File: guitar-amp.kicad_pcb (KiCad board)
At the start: 2 copper layers, 135 x 90 mm, 62 parts, among them J1 Speaker Output, J2 Input, J3 AC Mains, J4 Screw_Terminal_01x02, J5 Screw_Terminal_01x02, J6 Screw_Terminal_01x02, SW1 SW_SPST, T1 Transformer_1P_1S

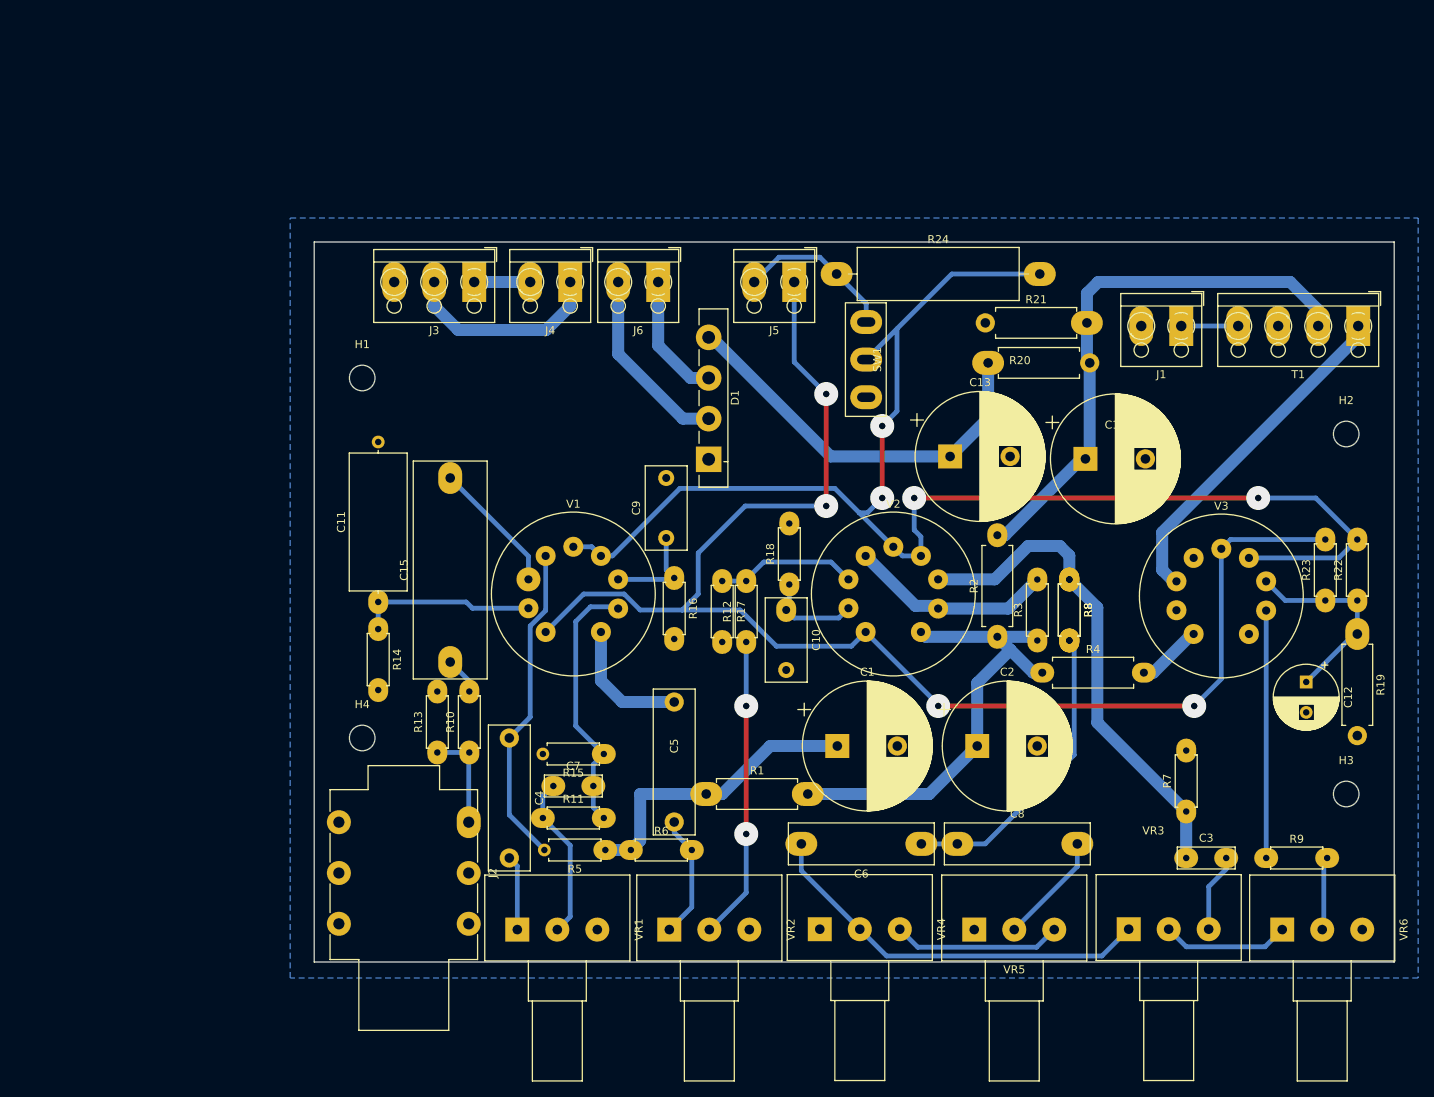
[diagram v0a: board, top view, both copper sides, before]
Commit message: update pads
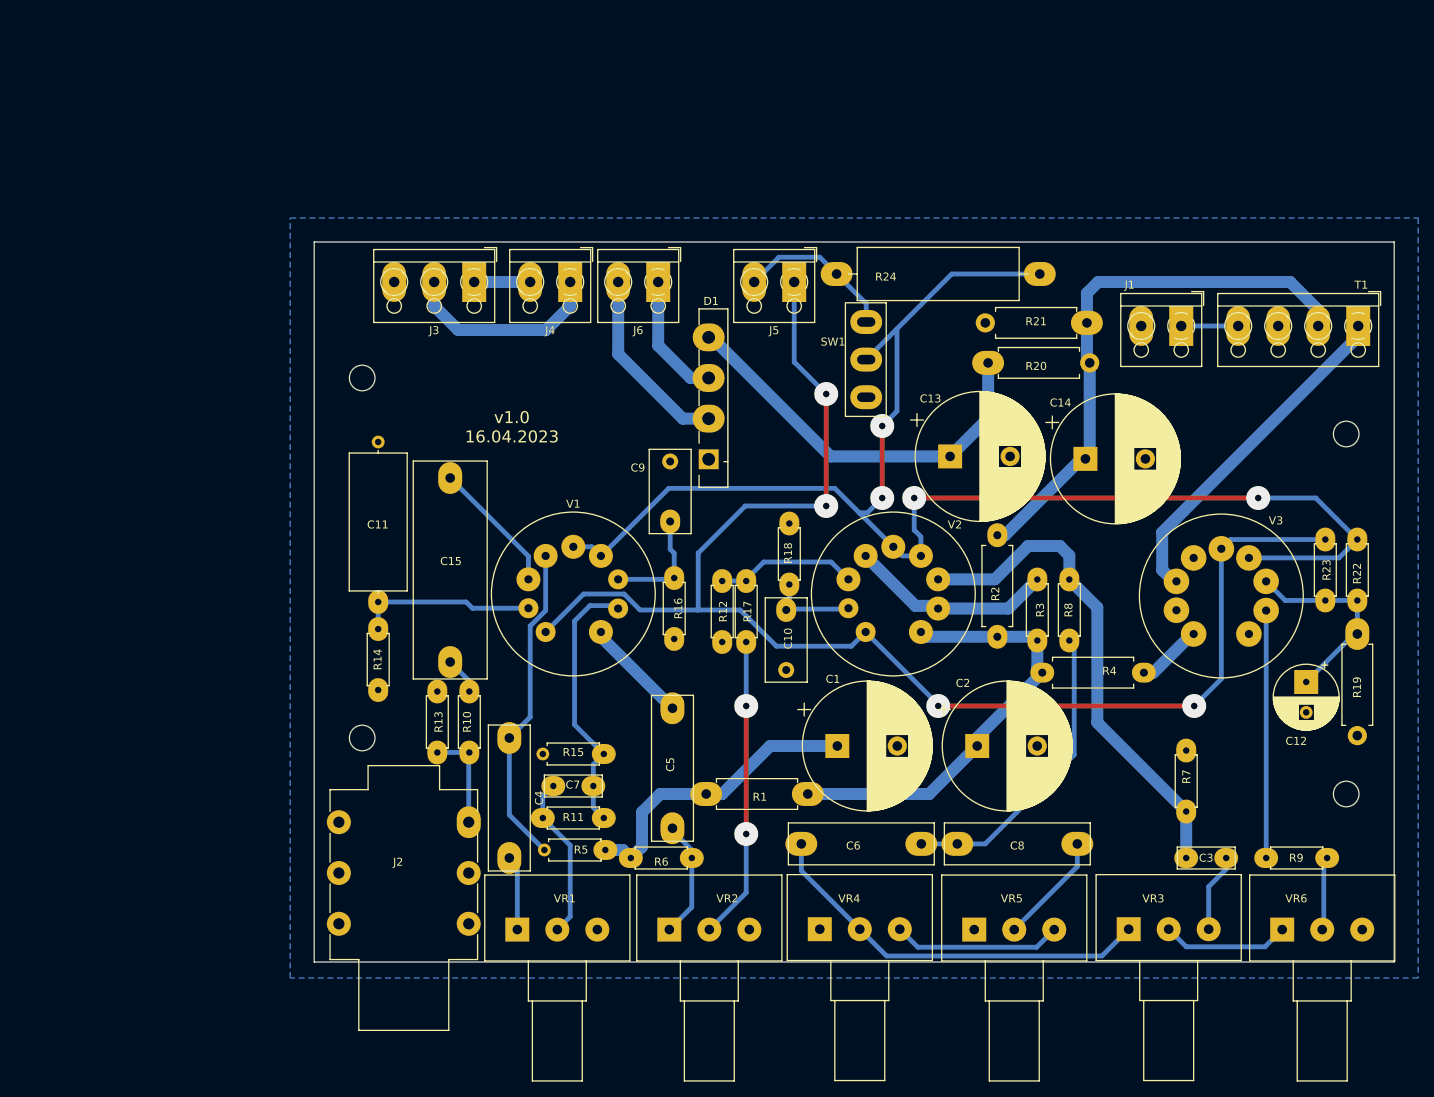
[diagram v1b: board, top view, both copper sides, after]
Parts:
- removed the R8 at (210.4, 92.2)
- moved C9 2.12 mm to (160.5, 84.9)
- moved R6 1.00 mm to (155.6, 127.0)
- moved C5 0.81 mm to (160.8, 108.3)
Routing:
- net /HighDC_241VDC: track 59.9 -> 55.5 mm
- net /HighDC_V1B_Anode: track 16.4 -> 13.2 mm
- net Net-(C9-Pad1): track 12.5 -> 14.4 mm
- net Net-(C10-Pad1): track 10.9 -> 10.0 mm
- net Net-(J5-Pad1): track 181.2 -> 180.4 mm
- net Net-(C5-Pad2): track 15.5 -> 14.8 mm
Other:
- board text added: "v1.0 16.04.2023"

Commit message: prepare for plotting
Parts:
- moved H2 10.0 mm to (246.0, 64.0)
- moved R9 7.81 mm to (235.0, 119.2), turned to -90 degrees
- moved H3 6.08 mm to (246.0, 125.0)
- moved J1 5.51 mm to (224.4, 55.0)
- moved T1 5.51 mm to (246.5, 55.0)
- moved R15 4.37 mm to (152.4, 118.4)
- moved C7 3.97 mm to (147.3, 114.3)
- moved H1 3.16 mm to (121.0, 64.0)
- moved H4 1.00 mm to (121.0, 112.0)
- moved R11 0.22 mm to (144.8, 121.9)
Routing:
- net Net-(R9-Pad1): track 30.9 -> 23.2 mm
- net /HighDC_OT: track 43.0 -> 48.3 mm
- net Net-(C7-Pad1): track 20.6 -> 25.6 mm
- net /HighDC_Post: track 68.9 -> 64.0 mm
- net Net-(R9-Pad2): track 9.21 -> 13.1 mm
- net Net-(C7-Pad2): track 33.6 -> 32.5 mm
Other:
- board text added: "Hole Size - All C and R 0.8 - Terminal sockets 1 - Potis 1 - Valves 1.02 - Bridge rectifier 1.2 - Jack socket 1.2"
- board text added: "TODO: - Buy 2 x 12AX7"

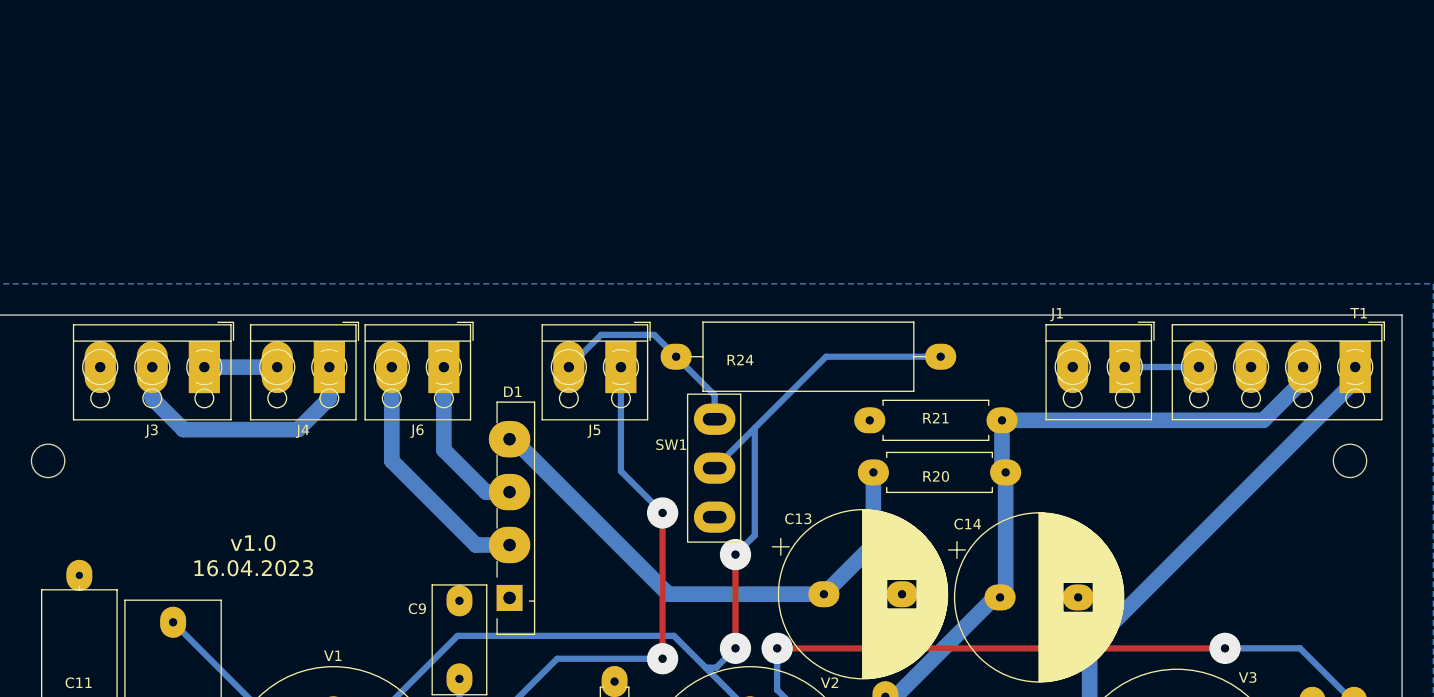
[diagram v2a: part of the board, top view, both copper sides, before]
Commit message: Add lamp and test points
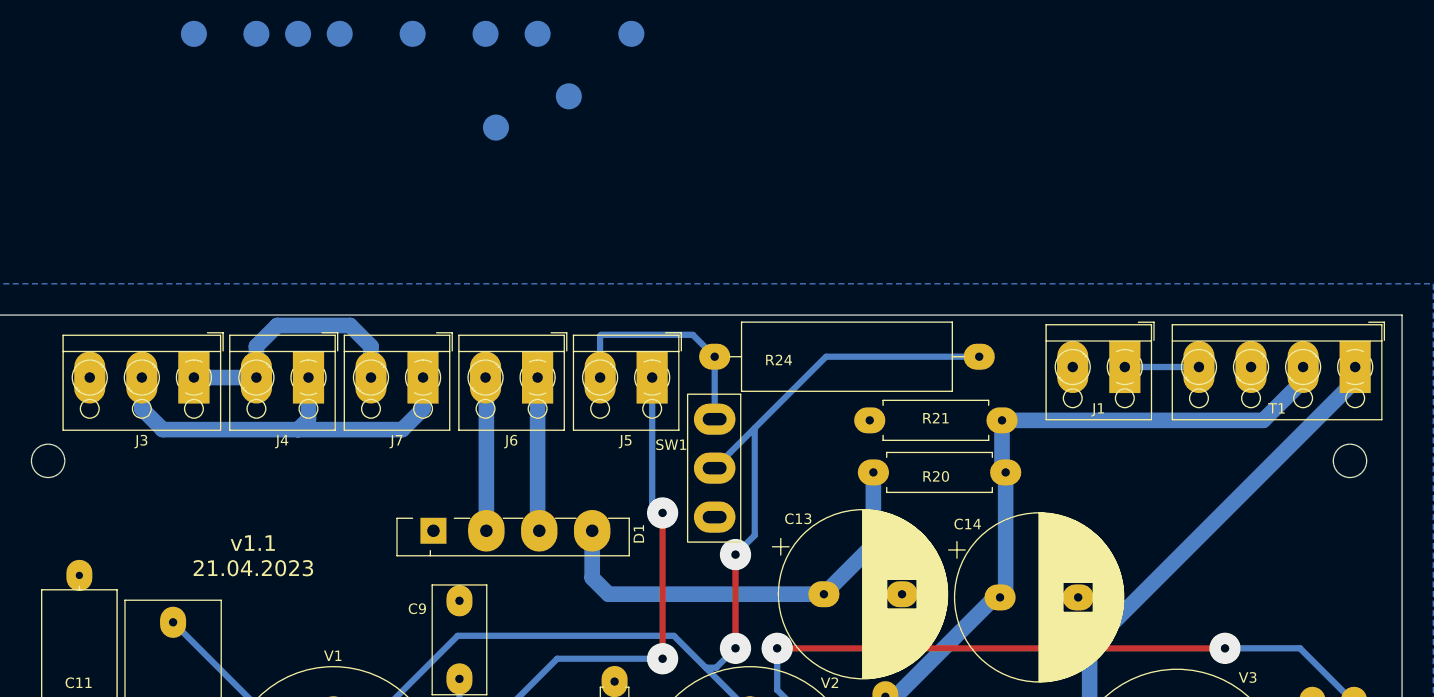
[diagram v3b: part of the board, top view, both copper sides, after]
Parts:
- added J7: Lamp, TerminalBlock_RND:TerminalBlock_RND_205-00001_1x02_P5.00mm_Horizontal, F.Cu at (157.0, 56.0)
- added TP1: TestPoint_Probe, TestPoint:TestPoint_Pad_D2.5mm, B.Cu at (135.0, 23.0)
- added TP10: TestPoint_Probe, TestPoint:TestPoint_Pad_D2.5mm, B.Cu at (177.0, 23.0)
- added TP2: TestPoint_Probe, TestPoint:TestPoint_Pad_D2.5mm, B.Cu at (141.0, 23.0)
- added TP3: TestPoint_Probe, TestPoint:TestPoint_Pad_D2.5mm, B.Cu at (145.0, 23.0)
- added TP4: TestPoint_Probe, TestPoint:TestPoint_Pad_D2.5mm, B.Cu at (149.0, 23.0)
- added TP5: TestPoint_Probe, TestPoint:TestPoint_Pad_D2.5mm, B.Cu at (156.0, 23.0)
- added TP6: TestPoint_Probe, TestPoint:TestPoint_Pad_D2.5mm, B.Cu at (163.0, 23.0)
- added TP7: TestPoint_Probe, TestPoint:TestPoint_Pad_D2.5mm, B.Cu at (164.0, 32.0)
- added TP8: TestPoint_Probe, TestPoint:TestPoint_Pad_D2.5mm, B.Cu at (168.0, 23.0)
- added TP9: TestPoint_Probe, TestPoint:TestPoint_Pad_D2.5mm, B.Cu at (171.0, 29.0)
- moved D1 9.75 mm to (158.0, 70.7), turned to 0 degrees
- moved J6 9.06 mm to (168.0, 56.0)
- moved R24 3.70 mm to (185.0, 54.0)
- moved J5 3.16 mm to (179.0, 56.0)
- moved J4 2.24 mm to (146.0, 56.0)
- moved J3 1.41 mm to (135.0, 56.0)
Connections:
- net Net-(J5-Pad1) renamed /HighCurrentTrace3
- net Net-(J5-Pad2) renamed /HighCurrentTrace1
- net Net-(R22-Pad2) renamed /HighCurrentTrace2
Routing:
- net /AC_L: track 7.00 -> 24.7 mm
- net /AC_N: track 25.5 -> 40.1 mm
- net /HighDC_Prefilter: track 50.0 -> 41.1 mm
- net /HighDC_Trafo1: track 23.7 -> 14.7 mm
- net /HighCurrentTrace2: track 182.2 -> 185.9 mm
- net /HighCurrentTrace3: track 180.4 -> 178.2 mm
- net /HighCurrentTrace1: track 20.0 -> 21.9 mm
- net /HighDC_Trafo2: track 15.9 -> 14.8 mm
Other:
- board text added: "v1.1 21.04.2023"
- board text removed: "TODO: - Buy 2 x 12AX7"
- board text removed: "v1.0 16.04.2023"

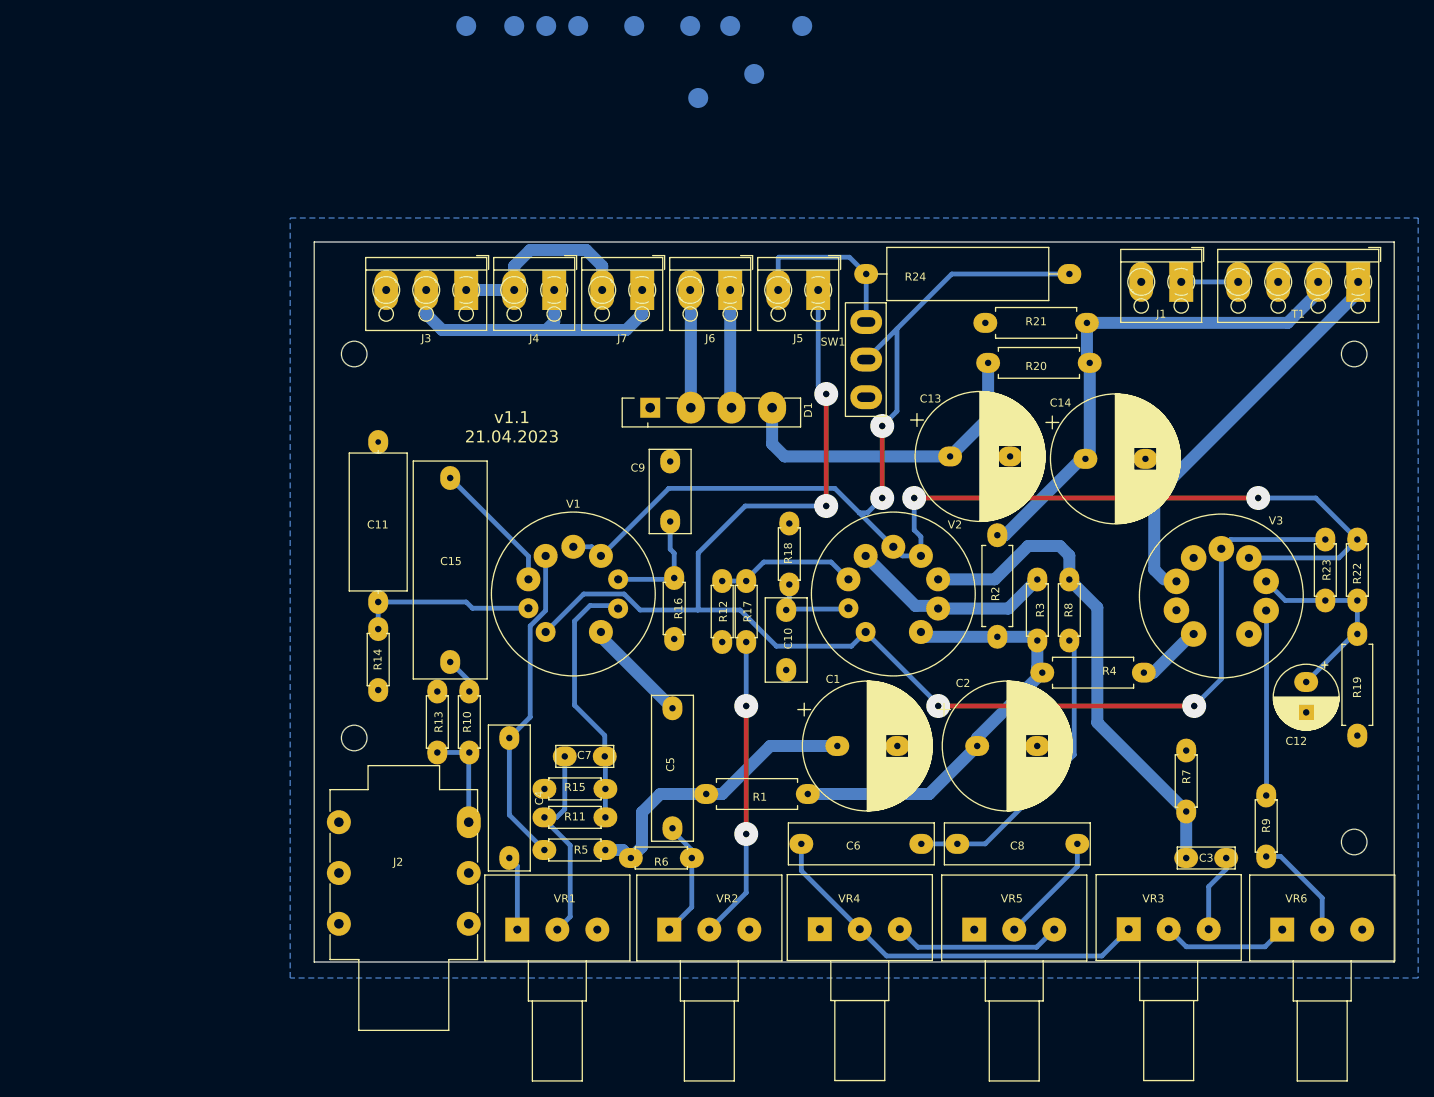
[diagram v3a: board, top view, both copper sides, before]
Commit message: Make the filament traces bigger
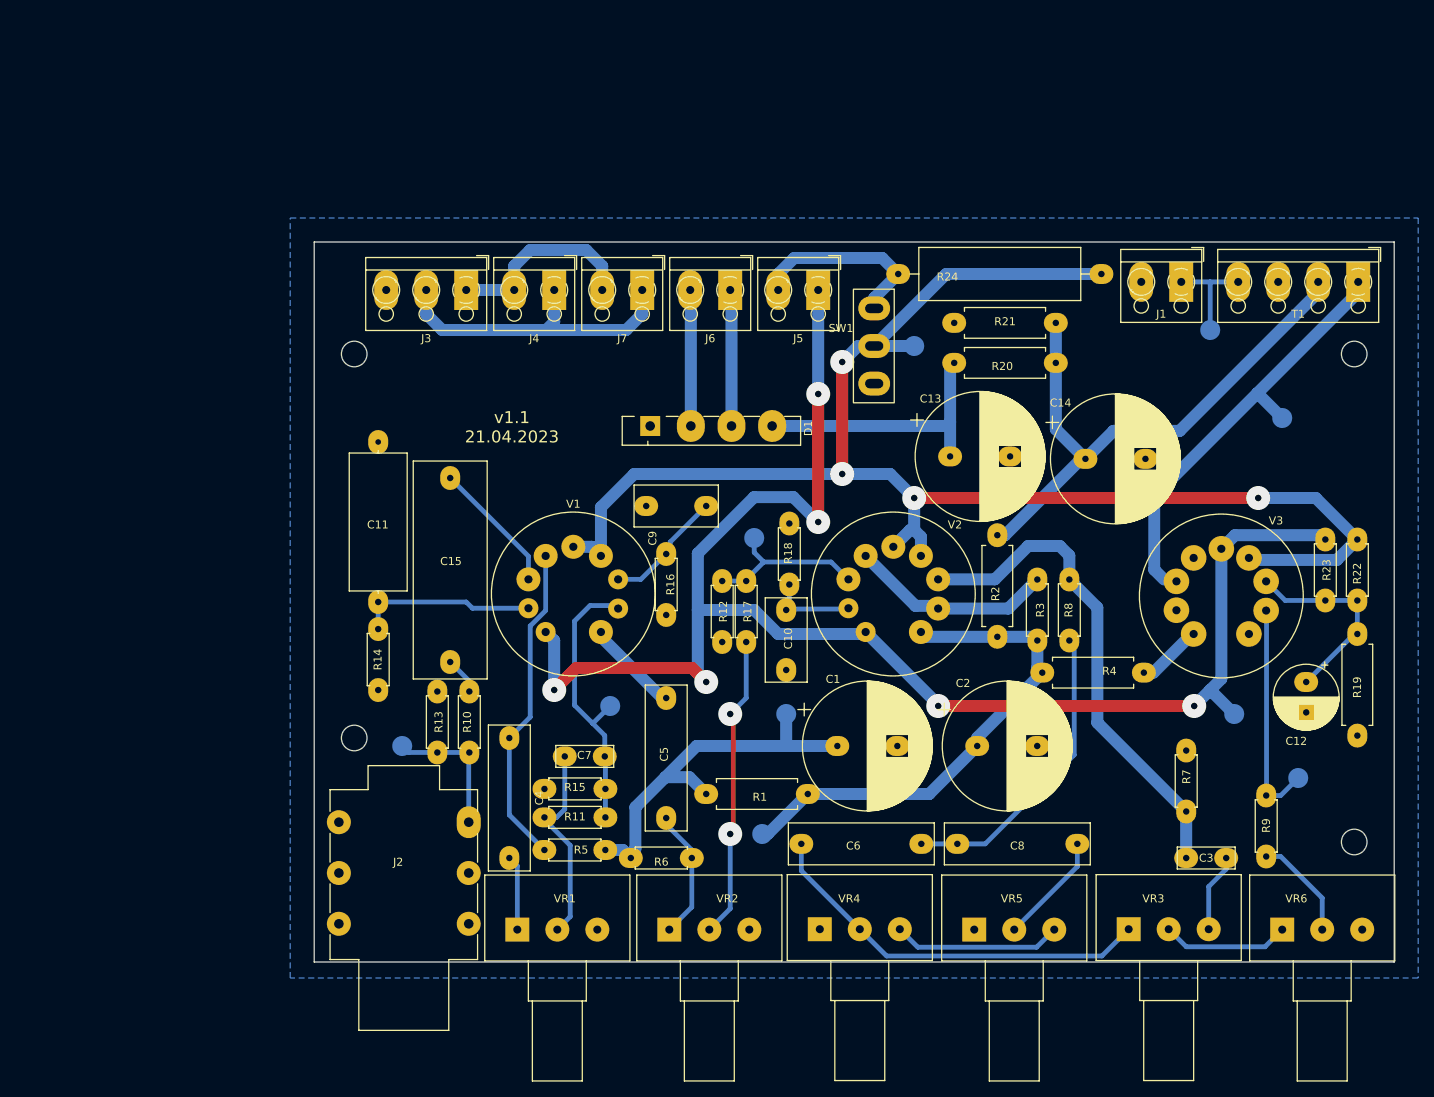
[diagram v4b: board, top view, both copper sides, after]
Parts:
- moved TP4 130.1 mm to (239.0, 117.0)
- moved TP8 106.6 mm to (231.0, 109.0)
- moved TP9 95.0 mm to (172.0, 124.0)
- moved TP1 90.4 mm to (127.0, 113.0)
- moved TP6 86.8 mm to (175.0, 109.0)
- moved TP2 85.8 mm to (153.0, 108.0)
- moved TP5 81.4 mm to (228.0, 61.0)
- moved TP10 77.5 mm to (237.0, 72.0)
- moved TP3 69.1 mm to (171.0, 87.0)
- moved TP7 41.1 mm to (191.0, 63.0)
- moved C9 4.90 mm to (165.0, 83.0), turned to 180 degrees
- moved R20 4.24 mm to (196.0, 65.1)
- moved R24 4.00 mm to (189.0, 54.0)
- moved R21 3.89 mm to (196.0, 60.1)
- moved R16 3.16 mm to (160.0, 89.0)
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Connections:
- J7 pad 1: /AC_L -> /AC_N
- J7 pad 2: /AC_N -> /AC_L
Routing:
- net /HighCurrentTrace3: track 178.2 -> 200.1 mm, vias 4 -> 6
- net /HighDC_227VDC: track 37.7 -> 48.6 mm
- net /HighDC_Post: track 64.0 -> 73.2 mm
- net /HighDC_241VDC: track 55.5 -> 63.2 mm
- net /HighDC_Prefilter: track 41.1 -> 34.4 mm
- net Net-(J1-Pad1): track 7.12 -> 13.1 mm
- net /HighCurrentTrace2: track 185.9 -> 191.0 mm
- net Net-(R9-Pad1): track 23.2 -> 28.1 mm
- net Net-(J2-PadT): track 12.7 -> 17.5 mm
- net /HighDC_OT: track 48.3 -> 52.6 mm
- net Net-(R12-Pad2): track 17.7 -> 21.2 mm
- net Net-(C7-Pad2): track 32.5 -> 35.6 mm
- net /HighCurrentTrace1: track 21.9 -> 24.2 mm
- net /HighDC_Trafo2: track 14.8 -> 17.1 mm
- net /HighDC_Trafo1: track 14.7 -> 17.0 mm
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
